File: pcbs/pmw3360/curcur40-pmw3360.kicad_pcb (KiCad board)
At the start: 2 copper layers, 29.6 x 29.2 mm, 13 parts, among them J1 SM06B-SRSS-TB, U1 PMW3360DM-T2QU, U2 TLV74318PDBVR

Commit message: fix(pmw3360): move R2 away from TB2 mounting hole to prevent case boss interference
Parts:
- moved R2 3.02 mm to (15.4, 41.7)
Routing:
- net /V_{IO}: track 35.9 -> 33.5 mm
- net /MISO: track 17.8 -> 17.0 mm
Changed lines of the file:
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@@
 	(footprint "Resistor_SMD:R_0603_1608Metric_Pad0.98x0.95mm_HandSolder"
 		(layer "B.Cu")
-		(at 17.886 43.3617)
+		(at 15.386 41.6617)
 		(descr "Resistor SMD 0603 (1608 Metric), square (rectangular) end terminal, IPC-7351 nominal with elongated pad for handsoldering. (Body size source: IPC-SM-782 page 72, https://www.pcb-3d.com/wordpress/wp-content/uploads/ipc-sm-782a_amendment_1_and_2.pdf)")
 		(tags "resistor handsolder")
@@
 	(segment
 		(start 2.7 51.4355)
-		(end 2.7 42.6)
+		(end 2.7 42.8)
 		(width 0.2)
 		(layer "F.Cu")
@@
 	)
 	(segment
-		(start 2.7 42.6)
-		(end 16.9735 42.6)
+		(start 2.7 42.8)
+		(end 14.4735 42.8)
 		(width 0.2)
 		(layer "F.Cu")
@@
 	)
 	(via
-		(at 16.9735 42.6)
+		(at 14.4735 42.8)
 		(size 0.6)
 		(drill 0.3)
@@
 	)
 	(segment
-		(start 16.9735 42.6)
-		(end 16.9735 43.3617)
+		(start 14.4735 42.8)
+		(end 14.4735 41.6617)
 		(width 0.2)
 		(layer "B.Cu")
@@
 	)
 	(segment
-		(start 16.2 50.5455)
-		(end 16.2 46)
+		(start 16.2985 50.5455)
+		(end 16.2985 43.5)
 		(width 0.2)
 		(layer "F.Cu")
@@
 	)
 	(segment
-		(start 16.2 46)
-		(end 18.7985 46)
+		(start 14.875 50.5455)
+		(end 16.2985 50.5455)
 		(width 0.2)
 		(layer "F.Cu")
 		(net "/MISO")
 	)
-	(segment
-		(start 14.875 50.5455)
-		(end 16.2 50.5455)
-		(width 0.2)
-		(layer "F.Cu")
-		(net "/MISO")
-	)
 	(via
-		(at 18.7985 46)
+		(at 16.2985 43.5)
 		(size 0.6)
 		(drill 0.3)
@@
 	)
 	(segment
-		(start 18.7985 46)
-		(end 18.7985 43.3617)
-		(width 0.2)
-		(layer "B.Cu")
+		(start 16.2985 43.5)
+		(end 16.2985 41.6617)
+		(width 0.2)
+		(layer "B.Cu")

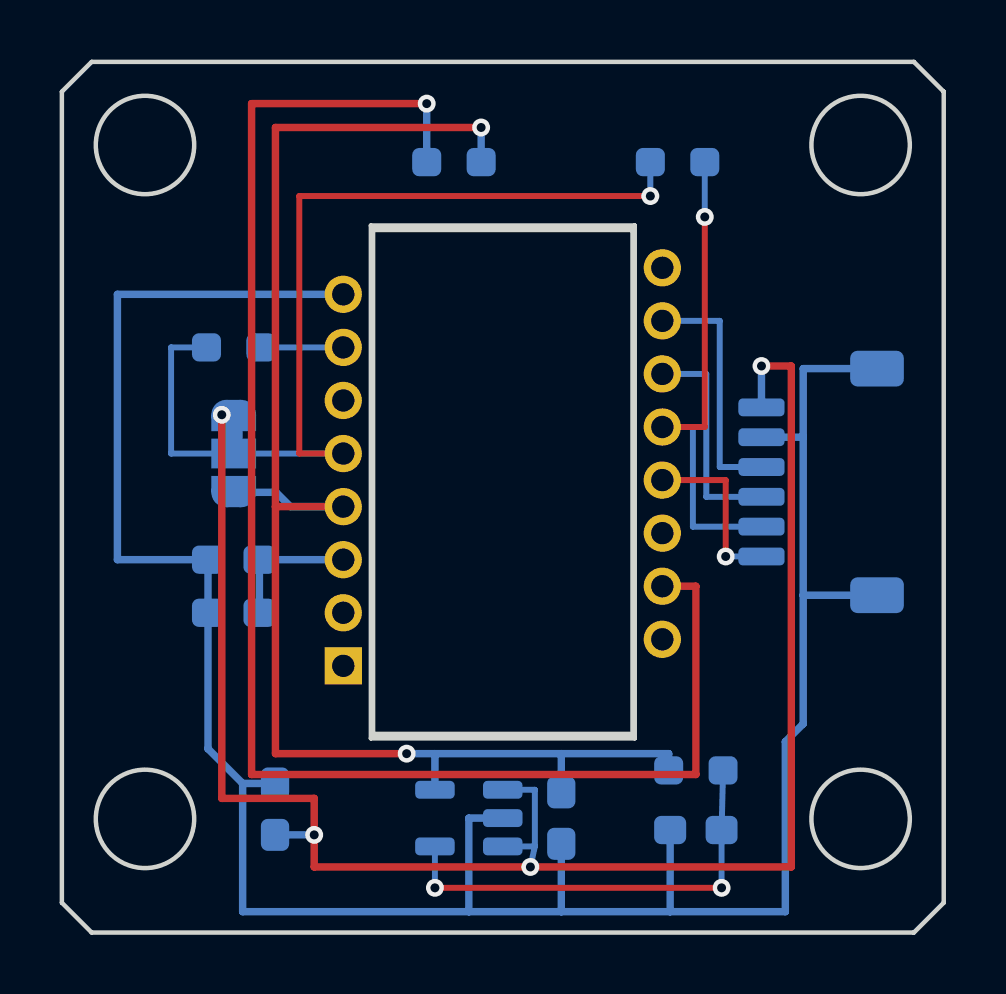
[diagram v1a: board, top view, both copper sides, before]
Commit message: fix(pmw3360): shift J1 1.0mm West and C3 0.5mm East to increase case floor & boss clearances
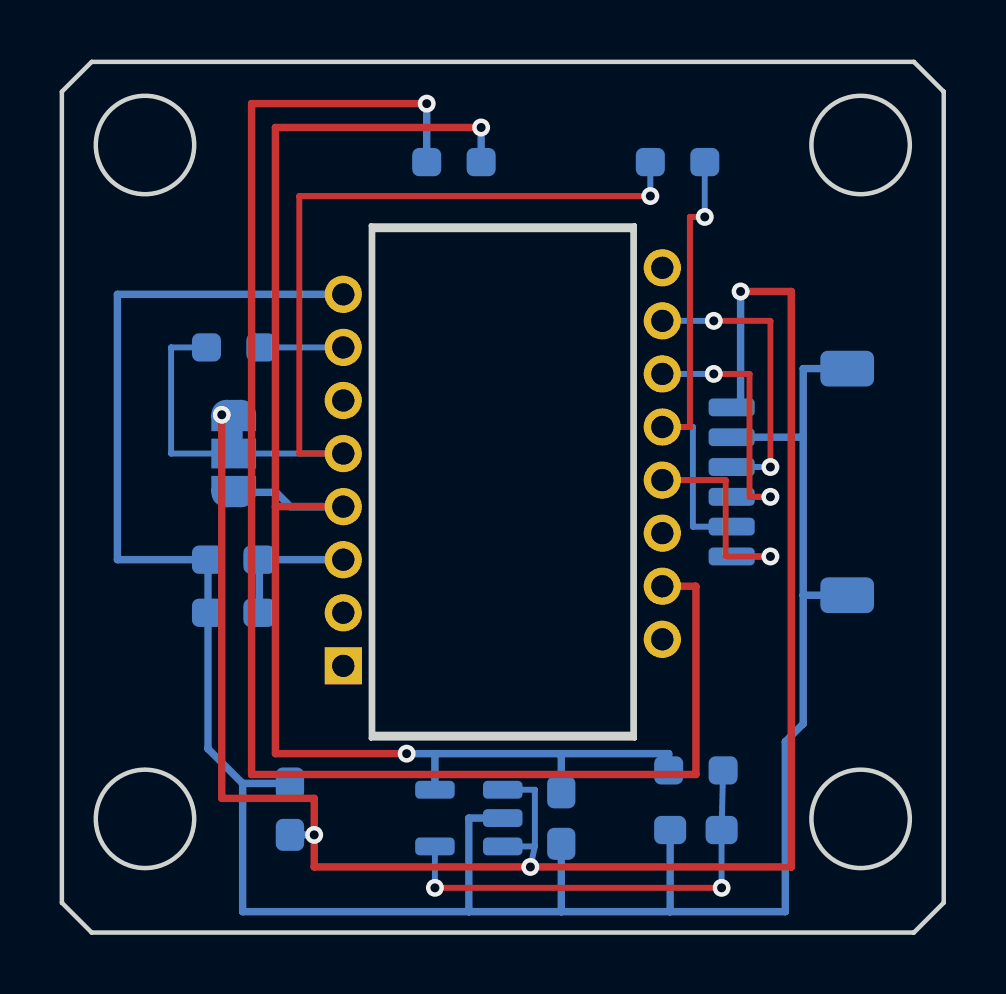
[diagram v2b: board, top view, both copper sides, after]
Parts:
- moved J1 1.00 mm to (19.2, 52.4)
- moved C3 0.50 mm to (2.39, 63.4)
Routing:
- net +3V3R: track 59.9 -> 65.4 mm
- net /SCLK: track 8.23 -> 9.83 mm, vias 0 -> 2
- net /NCS: track 5.89 -> 7.49 mm
- net /MOSI: track 7.45 -> 9.05 mm, vias 0 -> 2
- net /MISO: track 17.0 -> 16.0 mm
- net GNDR: track 85.2 -> 84.7 mm
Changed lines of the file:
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@@
 	(footprint "Capacitor_SMD:C_0603_1608Metric_Pad1.08x0.95mm_HandSolder"
 		(layer "B.Cu")
-		(at 1.886 63.3617 90)
+		(at 2.386 63.3617 90)
 		(descr "Capacitor SMD 0603 (1608 Metric), square (rectangular) end terminal, IPC-7351 nominal with elongated pad for handsoldering. (Body size source: IPC-SM-782 page 76, https://www.pcb-3d.com/wordpress/wp-content/uploads/ipc-sm-782a_amendment_1_and_2.pdf)")
 		(tags "capacitor handsolder")
@@
 	(footprint "Connector_JST:JST_SH_SM06B-SRSS-TB_1x06-1MP_P1.00mm_Horizontal"
 		(layer "B.Cu")
-		(at 20.2 52.3875 -90)
+		(at 19.2 52.3875 -90)
 		(descr "JST SH series connector, SM06B-SRSS-TB (http://www.jst-mfg.com/product/pdf/eng/eSH.pdf)")
 		(tags "connector JST SH horizontal")
@@
 	)
 	(segment
-		(start 19.2 48.5)
+		(start 19.2 46.0)
 		(end 19.2 65.3)
 		(width 0.25)
@@
 	)
 	(segment
-		(start 18.2 48.5)
-		(end 19.2 48.5)
+		(start 17.5 46.0)
+		(end 19.2 46.0)
 		(width 0.25)
 		(layer "F.Cu")
@@
 	)
 	(via
-		(at 18.2 48.5)
+		(at 17.5 46.0)
 		(size 0.6)
 		(drill 0.3)
@@
 	)
 	(segment
-		(start 18.2 49.8875)
-		(end 18.2 48.5)
+		(start 17.2 49.8875)
+		(end 17.5 49.8875)
+		(width 0.25)
+		(layer "B.Cu")
+		(net "+3V3R")
+	)
+	(segment
+		(start 17.5 49.8875)
+		(end 17.5 46.0)
 		(width 0.25)
 		(layer "B.Cu")
@@
 	(segment
 		(start 3.2 64.224199)
-		(end 1.886 64.224199)
+		(end 2.386 64.224199)
 		(width 0.25)
 		(layer "B.Cu")
@@
 	)
 	(segment
-		(start 18.2 50.8875)
+		(start 17.2 50.8875)
 		(end 19.6 50.8875)
 		(width 0.25)
@@
 	(segment
 		(start 19.6 56.1875)
-		(end 22.075 56.1875)
+		(end 21.075 56.1875)
 		(width 0.25)
 		(layer "B.Cu")
@@
 	(segment
 		(start 19.6 48.5875)
-		(end 22.075 48.5875)
+		(end 21.075 48.5875)
 		(width 0.25)
 		(layer "B.Cu")
@@
 	(segment
 		(start 0.8 62.4992)
-		(end 1.886 62.4992)
+		(end 2.386 62.4992)
 		(width 0.25)
 		(layer "B.Cu")
@@
 	(segment
 		(start 14.875 46.9855)
-		(end 16.8 46.9855)
+		(end 16.6 46.9855)
 		(width 0.2)
 		(layer "B.Cu")
 		(net "/SCLK")
 	)
+	(via
+		(at 16.6 46.9855)
+		(size 0.6)
+		(drill 0.3)
+		(layers "F.Cu" "B.Cu")
+		(net "/SCLK")
+	)
 	(segment
-		(start 16.8 51.8875)
-		(end 18.2 51.8875)
+		(start 16.6 46.9855)
+		(end 18.5 46.9855)
 		(width 0.2)
-		(layer "B.Cu")
+		(layer "F.Cu")
+		(net "/SCLK")
+	)
+	(segment
+		(start 18.5 46.9855)
+		(end 18.5 51.8875)
+		(width 0.2)
+		(layer "F.Cu")
+		(net "/SCLK")
+	)
+	(via
+		(at 18.5 51.8875)
+		(size 0.6)
+		(drill 0.3)
+		(layers "F.Cu" "B.Cu")
 		(net "/SCLK")
 	)
 	(segment
-		(start 16.8 46.9855)
-		(end 16.8 51.8875)
+		(start 18.5 51.8875)
+		(end 17.2 51.8875)
 		(width 0.2)
 		(layer "B.Cu")
@@
 	)
 	(segment
-		(start 16.35 48.7655)
-		(end 16.35 52.8875)
+		(start 14.875 48.7655)
+		(end 16.6 48.7655)
 		(width 0.2)
 		(layer "B.Cu")
 		(net "/MOSI")
 	)
+	(via
+		(at 16.6 48.7655)
+		(size 0.6)
+		(drill 0.3)
+		(layers "F.Cu" "B.Cu")
+		(net "/MOSI")
+	)
 	(segment
-		(start 16.35 52.8875)
-		(end 18.2 52.8875)
+		(start 16.6 48.7655)
+		(end 17.8 48.7655)
 		(width 0.2)
-		(layer "B.Cu")
+		(layer "F.Cu")
 		(net "/MOSI")
 	)
 	(segment
-		(start 14.875 48.7655)
-		(end 16.35 48.7655)
+		(start 17.8 48.7655)
+		(end 17.8 52.8875)
+		(width 0.2)
+		(layer "F.Cu")
+		(net "/MOSI")
+	)
+	(segment
+		(start 17.8 52.8875)
+		(end 18.5 52.8875)
+		(width 0.2)
+		(layer "F.Cu")
+		(net "/MOSI")
+	)
+	(via
+		(at 18.5 52.8875)
+		(size 0.6)
+		(drill 0.3)
+		(layers "F.Cu" "B.Cu")
+		(net "/MOSI")
+	)
+	(segment
+		(start 18.5 52.8875)
+		(end 17.2 52.8875)
 		(width 0.2)
 		(layer "B.Cu")
@@
 	)
 	(segment
-		(start 16.2985 50.5455)
-		(end 16.2985 43.5)
+		(start 15.8 50.5455)
+		(end 15.8 43.5)
 		(width 0.2)
 		(layer "F.Cu")
@@
 	(segment
 		(start 14.875 50.5455)
-		(end 16.2985 50.5455)
+		(end 15.8 50.5455)
+		(width 0.2)
+		(layer "F.Cu")
+		(net "/MISO")
+	)
+	(segment
+		(start 15.8 43.5)
+		(end 16.2985 43.5)
 		(width 0.2)
 		(layer "F.Cu")
@@
 	(segment
 		(start 15.9 53.8875)
-		(end 18.2 53.8875)
+		(end 17.2 53.8875)
 		(width 0.2)
 		(layer "B.Cu")
@@
 		(net "/NCS")
 	)
+	(segment
+		(start 17 54.8875)
+		(end 18.5 54.8875)
+		(width 0.2)
+		(layer "F.Cu")
+		(net "/NCS")
+	)
 	(via
-		(at 17 54.8875)
+		(at 18.5 54.8875)
 		(size 0.6)
 		(drill 0.3)
@@
 	)
 	(segment
-		(start 17 54.8875)
-		(end 18.2 54.8875)
+		(start 18.5 54.8875)
+		(end 17.2 54.8875)
 		(width 0.2)
 		(layer "B.Cu")
